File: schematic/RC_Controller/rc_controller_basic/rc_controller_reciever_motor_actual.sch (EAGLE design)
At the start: 19 parts, among them IC1 ATMEGA328-20P, SW1 CT10-XXXX-A2

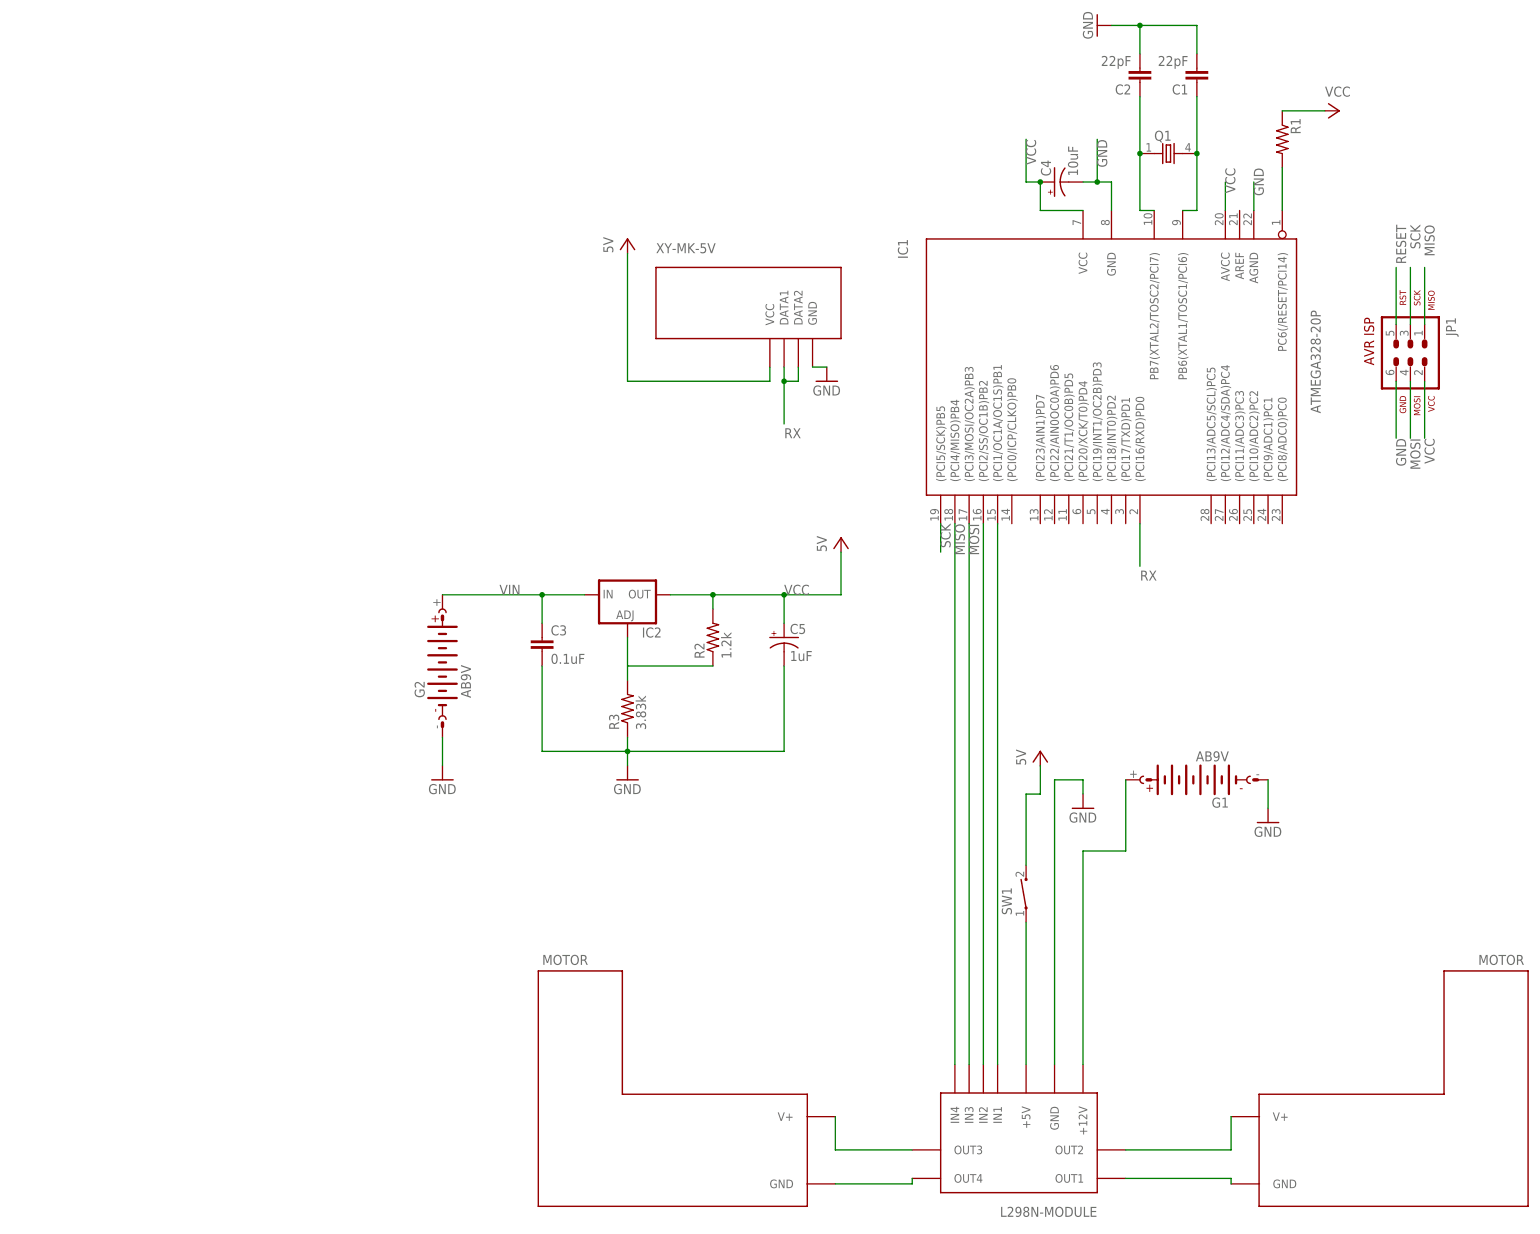
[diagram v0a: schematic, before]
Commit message: updated schematics
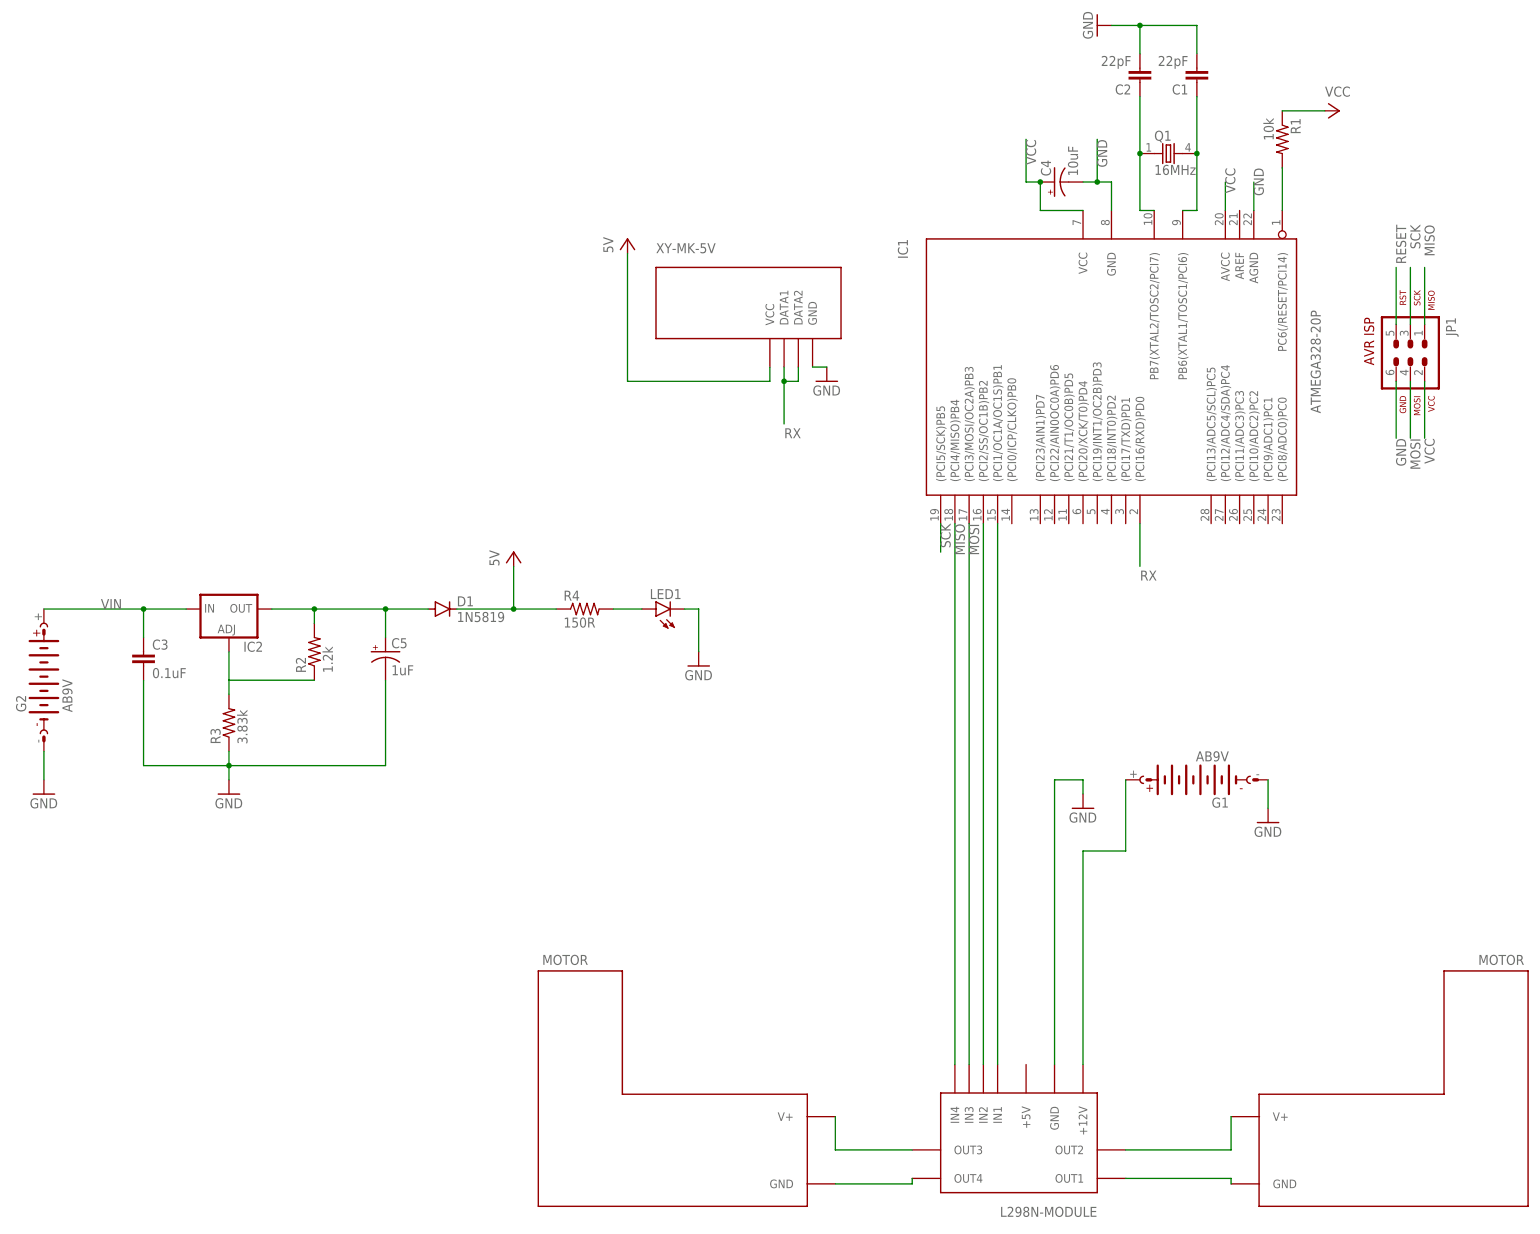
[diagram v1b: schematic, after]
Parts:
- removed SW1: CT10-XXXX-A2, switch-coto:CT10-XXXX-A2
- added D1: 1N5819, diode:1N4004
- added LED1: LAP4-BOTTOM, led:LAP4-BOTTOM
- added R4: 150R, rcl:R-US_0204/7
- Q1: value (none) -> 16MHz
- R1: value (none) -> 10k
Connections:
- removed net N$2: SW1.1, U$2.+5V
- new net N$12: C5.+, D1.A, IC2.OUT, R2.2
- new net N$13: LED1.A, R4.2
- net GND: now also LED1.C
- net VCC: now also D1.C, R4.1; no longer C5.+, IC2.OUT, R2.2, SW1.2
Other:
- moved on the sheet: C3, C5, G2, IC2, R2, R3
